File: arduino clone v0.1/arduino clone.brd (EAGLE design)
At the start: 72.9 x 27.6 mm, 47 parts, among them J203 ICSP HEADER, J402 FTDI Breakout Header, U101 ATMEGA328P_TQFP, U301 CH340G, Y101 16MHz, Y301 12MHz

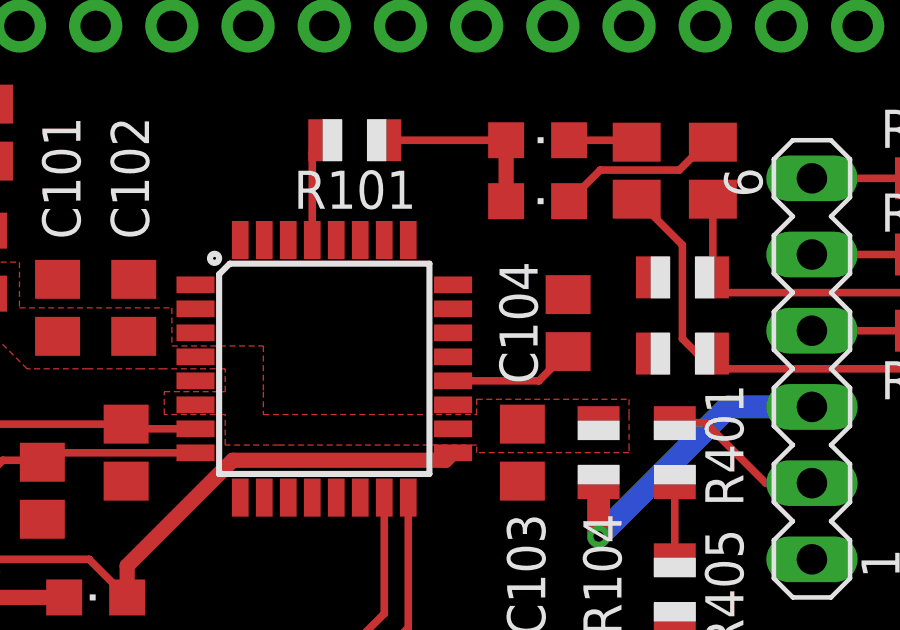
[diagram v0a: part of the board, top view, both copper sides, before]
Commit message: route PP5V0_MCU to UART LEDs
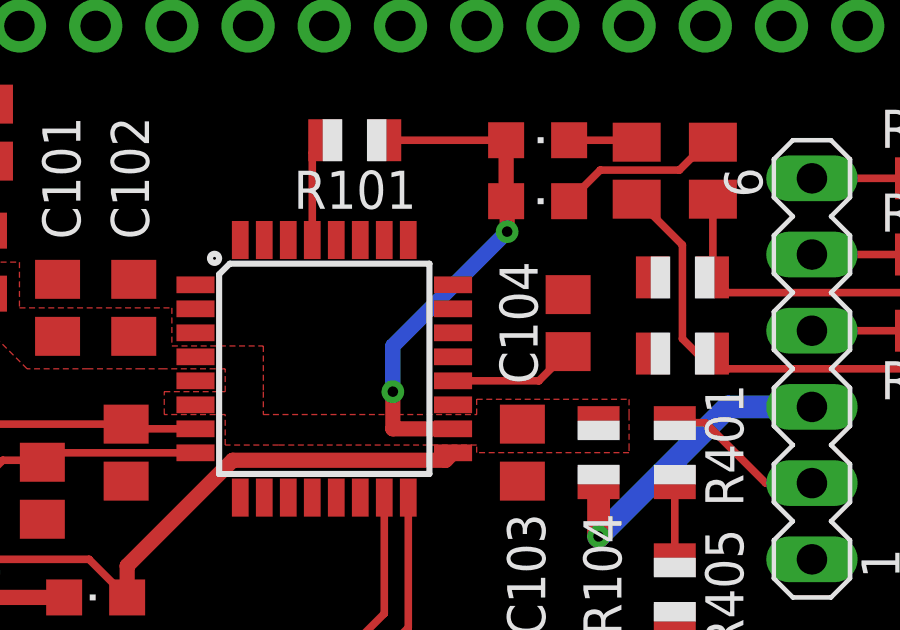
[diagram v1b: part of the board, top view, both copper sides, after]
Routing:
- net PP5V0_MCU: track 26.0 -> 37.2 mm, vias 2 -> 4
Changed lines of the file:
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@@
 <wire x1="40.352" y1="59.69" x2="40.352" y2="57.658" width="0.508" layer="1"/>
 <wire x1="36.306" y1="59.69" x2="40.352" y2="59.69" width="0.254" layer="1"/>
-<wire x1="40.894" y1="50.226" x2="40.352" y2="57.658" width="0" layer="19" extent="1-1"/>
+<wire x1="40.352" y1="57.658" x2="40.386" y2="57.624" width="0.508" layer="1"/>
+<wire x1="40.386" y1="57.624" x2="40.386" y2="56.642" width="0.508" layer="1"/>
+<via x="40.386" y="56.642" extent="1-16" drill="0.35"/>
+<wire x1="40.386" y1="56.642" x2="36.576" y2="52.832" width="0.508" layer="16"/>
+<wire x1="36.576" y1="52.832" x2="36.576" y2="51.308" width="0.508" layer="16"/>
+<via x="36.576" y="51.308" extent="1-16" drill="0.35"/>
+<wire x1="36.576" y1="51.308" x2="36.576" y2="50.07" width="0.508" layer="1"/>
+<wire x1="36.576" y1="50.07" x2="38.5826" y2="50.07" width="0.508" layer="1"/>
 </signal>
 <signal name="GND">

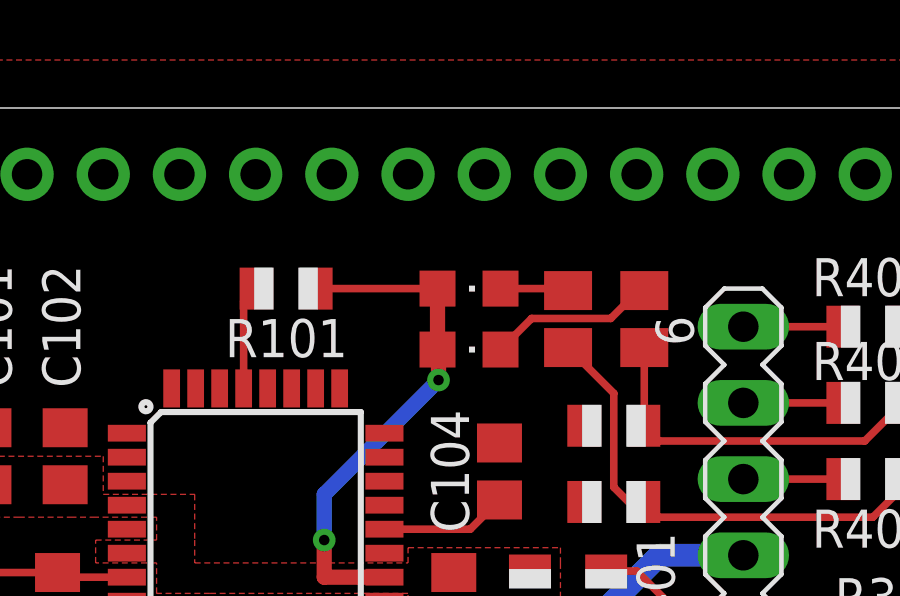
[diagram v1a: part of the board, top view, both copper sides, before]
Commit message: route analog pins 2-5
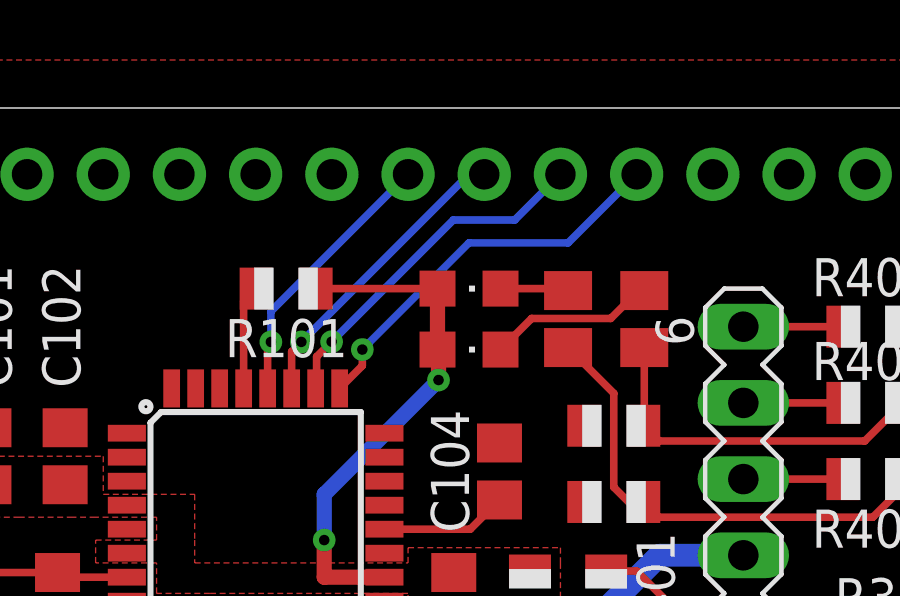
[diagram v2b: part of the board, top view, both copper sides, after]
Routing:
- net MCU_A2: track 0.00 -> 13.2 mm, vias 0 -> 1
- net MCU_A3: track 0.00 -> 11.7 mm, vias 0 -> 1
- net MCU_A4: track 0.00 -> 10.1 mm, vias 0 -> 1
- net MCU_A5: track 0.00 -> 9.08 mm, vias 0 -> 1
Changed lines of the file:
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@@
 <contactref element="R103" pad="2"/>
 <contactref element="J201" pad="1"/>
-<wire x1="32.29" y1="56.3626" x2="45.228" y2="55.118" width="0" layer="19" extent="1-1"/>
+<wire x1="45.228" y1="55.118" x2="32.29" y2="56.3626" width="0" layer="19" extent="1-1"/>
 <wire x1="24.13" y1="40.64" x2="32.29" y2="56.3626" width="0" layer="19" extent="1-1"/>
 </signal>
@@
 <contactref element="U101" pad="25"/>
 <contactref element="J202" pad="10"/>
-<wire x1="37.09" y1="56.3626" x2="46.99" y2="63.5" width="0" layer="19" extent="1-1"/>
+<wire x1="37.846" y1="57.1186" x2="37.846" y2="57.658" width="0.254" layer="1"/>
+<via x="37.846" y="57.658" extent="1-16" drill="0.35"/>
+<wire x1="37.846" y1="57.658" x2="41.402" y2="61.214" width="0.254" layer="16"/>
+<wire x1="41.402" y1="61.214" x2="44.704" y2="61.214" width="0.254" layer="16"/>
+<wire x1="44.704" y1="61.214" x2="46.99" y2="63.5" width="0.254" layer="16"/>
+<wire x1="37.09" y1="56.3626" x2="37.846" y2="57.1186" width="0.254" layer="1"/>
 </signal>
 <signal name="MCU_A5">
 <contactref element="U101" pad="28"/>
 <contactref element="J202" pad="7"/>
-<wire x1="34.69" y1="56.3626" x2="39.37" y2="63.5" width="0" layer="19" extent="1-1"/>
+<wire x1="34.69" y1="56.3626" x2="34.69" y2="57.804" width="0.254" layer="1"/>
+<wire x1="34.69" y1="57.804" x2="34.798" y2="57.912" width="0.254" layer="1"/>
+<via x="34.798" y="57.912" extent="1-16" drill="0.35"/>
+<wire x1="34.798" y1="57.912" x2="34.798" y2="58.928" width="0.254" layer="16"/>
+<wire x1="34.798" y1="58.928" x2="39.37" y2="63.5" width="0.254" layer="16"/>
 </signal>
 <signal name="MCU_A6">
@@
 <contactref element="U101" pad="27"/>
 <contactref element="J202" pad="8"/>
-<wire x1="35.49" y1="56.3626" x2="41.91" y2="63.5" width="0" layer="19" extent="1-1"/>
+<wire x1="35.49" y1="56.3626" x2="35.49" y2="57.588" width="0.254" layer="1"/>
+<wire x1="35.49" y1="57.588" x2="35.814" y2="57.912" width="0.254" layer="1"/>
+<via x="35.814" y="57.912" extent="1-16" drill="0.35"/>
+<wire x1="41.402" y1="63.5" x2="41.91" y2="63.5" width="0.254" layer="16"/>
+<wire x1="35.814" y1="57.912" x2="41.402" y2="63.5" width="0.254" layer="16"/>
 </signal>
 <signal name="MCU_A3">
 <contactref element="U101" pad="26"/>
 <contactref element="J202" pad="9"/>
-<wire x1="36.29" y1="56.3626" x2="44.45" y2="63.5" width="0" layer="19" extent="1-1"/>
+<wire x1="36.29" y1="56.3626" x2="36.322" y2="56.3946" width="0.254" layer="1"/>
+<wire x1="36.322" y1="56.3946" x2="36.322" y2="57.4192375" width="0.254" layer="1"/>
+<wire x1="36.82238125" y1="57.91961875" x2="36.322" y2="57.4192375" width="0.254" layer="1"/>
+<via x="36.82238125" y="57.91961875" extent="1-16" drill="0.35"/>
+<wire x1="36.82238125" y1="57.91961875" x2="40.8787625" y2="61.976" width="0.254" layer="16"/>
+<wire x1="40.8787625" y1="61.976" x2="42.926" y2="61.976" width="0.254" layer="16"/>
+<wire x1="42.926" y1="61.976" x2="44.45" y2="63.5" width="0.254" layer="16"/>
 </signal>
 <signal name="MCU_D2">
@@
 <contactref element="R102" pad="2"/>
 <contactref element="J201" pad="2"/>
-<wire x1="33.09" y1="56.3626" x2="45.228" y2="52.578" width="0" layer="19" extent="1-1"/>
+<wire x1="45.228" y1="52.578" x2="33.09" y2="56.3626" width="0" layer="19" extent="1-1"/>
 <wire x1="26.67" y1="40.64" x2="33.09" y2="56.3626" width="0" layer="19" extent="1-1"/>
 </signal>

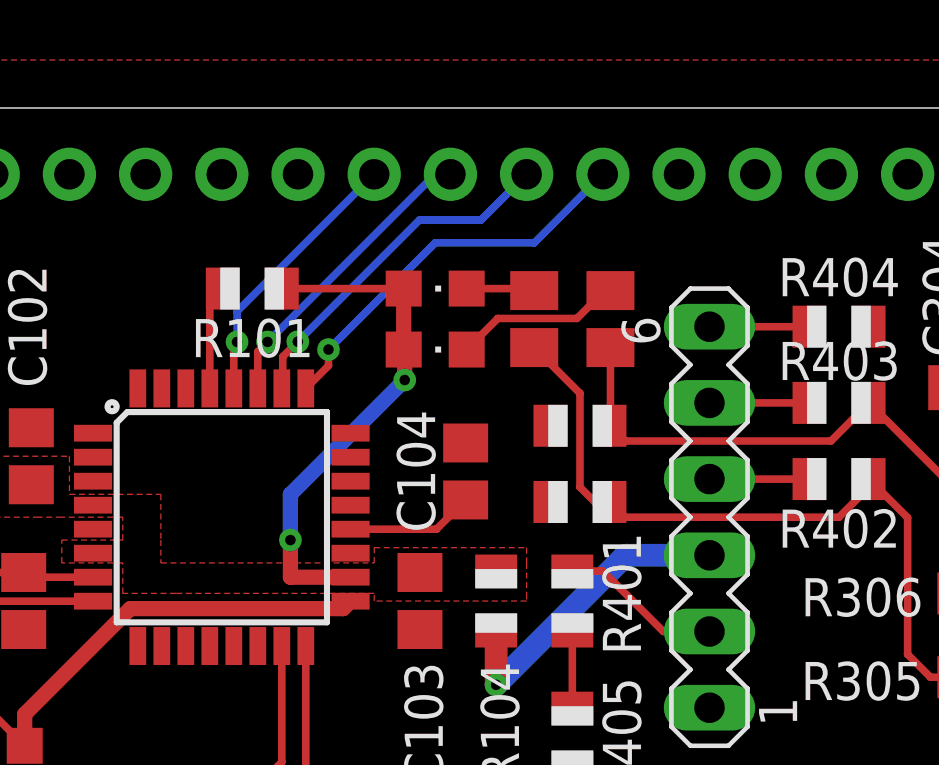
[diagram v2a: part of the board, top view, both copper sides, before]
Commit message: connect rest of analog pins
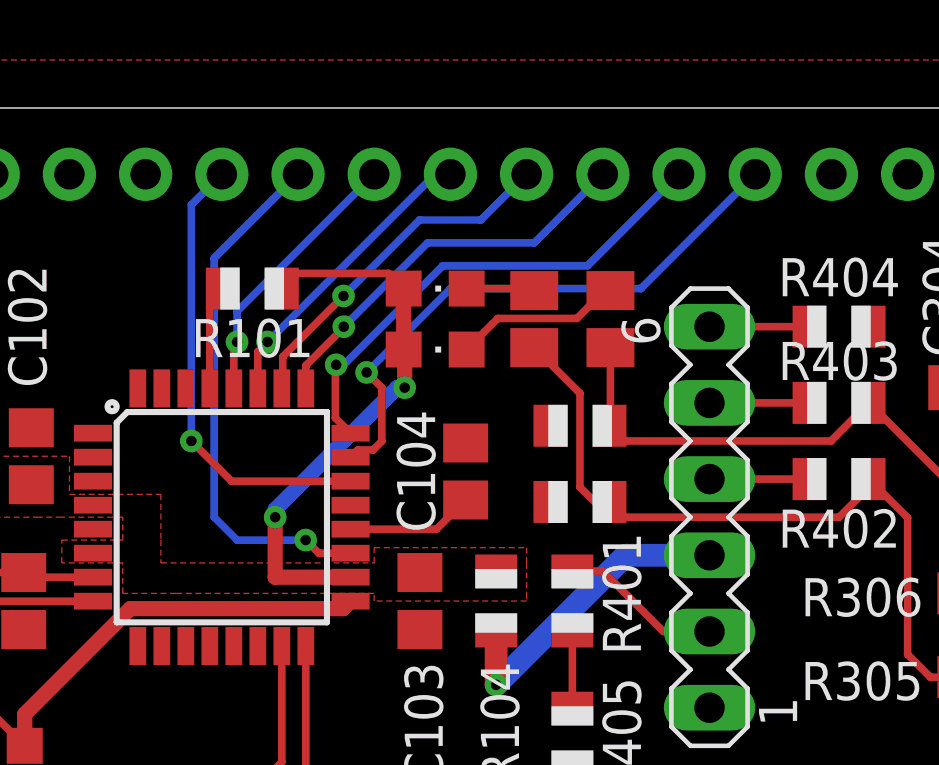
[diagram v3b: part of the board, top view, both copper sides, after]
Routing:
- net MCU_A0: track 0.00 -> 19.5 mm, vias 0 -> 1
- net MCU_A6: track 0.00 -> 17.6 mm, vias 0 -> 1
- net MCU_A1: track 0.00 -> 16.6 mm, vias 0 -> 1
- net MCU_A7: track 0.00 -> 15.2 mm, vias 0 -> 1
- net PP5V0_MCU: track 37.2 -> 38.5 mm
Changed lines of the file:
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@@
 <wire x1="16.51" y1="54.61" x2="21.59" y2="54.61" width="0.254" layer="16"/>
 <wire x1="40.352" y1="59.69" x2="40.352" y2="57.658" width="0.508" layer="1"/>
-<wire x1="36.306" y1="59.69" x2="40.352" y2="59.69" width="0.254" layer="1"/>
+<wire x1="36.814" y1="60.198" x2="39.844" y2="60.198" width="0.254" layer="1"/>
 <wire x1="40.352" y1="57.658" x2="40.386" y2="57.624" width="0.508" layer="1"/>
-<wire x1="40.386" y1="57.624" x2="40.386" y2="56.642" width="0.508" layer="1"/>
-<via x="40.386" y="56.642" extent="1-16" drill="0.35"/>
-<wire x1="40.386" y1="56.642" x2="36.576" y2="52.832" width="0.508" layer="16"/>
-<wire x1="36.576" y1="52.832" x2="36.576" y2="51.308" width="0.508" layer="16"/>
-<via x="36.576" y="51.308" extent="1-16" drill="0.35"/>
-<wire x1="36.576" y1="51.308" x2="36.576" y2="50.07" width="0.508" layer="1"/>
-<wire x1="36.576" y1="50.07" x2="38.5826" y2="50.07" width="0.508" layer="1"/>
+<wire x1="40.386" y1="57.624" x2="40.386" y2="56.388" width="0.508" layer="1"/>
+<via x="40.386" y="56.388" extent="1-16" drill="0.35"/>
+<wire x1="40.132" y1="56.388" x2="36.068" y2="52.324" width="0.508" layer="16"/>
+<wire x1="36.068" y1="52.324" x2="36.068" y2="52.07" width="0.508" layer="16"/>
+<via x="36.068" y="52.07" extent="1-16" drill="0.35"/>
+<wire x1="36.068" y1="52.07" x2="36.068" y2="50.07" width="0.508" layer="1"/>
+<wire x1="36.068" y1="50.07" x2="38.5826" y2="50.07" width="0.508" layer="1"/>
+<wire x1="36.306" y1="59.69" x2="36.814" y2="60.198" width="0.254" layer="1"/>
+<wire x1="39.844" y1="60.198" x2="40.352" y2="59.69" width="0.254" layer="1"/>
+<wire x1="40.386" y1="56.388" x2="40.132" y2="56.388" width="0.508" layer="16"/>
 </signal>
 <signal name="GND">
@@
 <contactref element="R103" pad="2"/>
 <contactref element="J201" pad="1"/>
-<wire x1="45.228" y1="55.118" x2="32.29" y2="56.3626" width="0" layer="19" extent="1-1"/>
+<wire x1="32.29" y1="56.3626" x2="45.228" y2="55.118" width="0" layer="19" extent="1-1"/>
 <wire x1="24.13" y1="40.64" x2="32.29" y2="56.3626" width="0" layer="19" extent="1-1"/>
 </signal>
@@
 <contactref element="U101" pad="23"/>
 <contactref element="J202" pad="12"/>
-<wire x1="38.5826" y1="54.07" x2="52.07" y2="63.5" width="0" layer="19" extent="1-1"/>
+<wire x1="38.5826" y1="54.07" x2="38.8238" y2="54.3112" width="0.254" layer="1"/>
+<wire x1="38.8238" y1="54.3112" x2="39.33333125" y2="54.3112" width="0.254" layer="1"/>
+<wire x1="39.33333125" y1="54.3112" x2="39.624" y2="54.60186875" width="0.254" layer="1"/>
+<wire x1="39.624" y1="56.388" x2="39.116" y2="56.896" width="0.254" layer="1"/>
+<via x="39.116" y="56.896" extent="1-16" drill="0.35"/>
+<wire x1="39.116" y1="56.896" x2="41.91" y2="59.69" width="0.254" layer="16"/>
+<wire x1="48.26" y1="59.69" x2="52.07" y2="63.5" width="0.254" layer="16"/>
+<wire x1="39.624" y1="54.60186875" x2="39.624" y2="56.388" width="0.254" layer="1"/>
+<wire x1="41.91" y1="59.69" x2="48.26" y2="59.69" width="0.254" layer="16"/>
 </signal>
 <signal name="MCU_A1">
 <contactref element="U101" pad="24"/>
 <contactref element="J202" pad="11"/>
-<wire x1="38.5826" y1="54.87" x2="49.53" y2="63.5" width="0" layer="19" extent="1-1"/>
+<wire x1="38.0746" y1="55.378" x2="38.0746" y2="57.1246" width="0.254" layer="1"/>
+<via x="38.1" y="57.15" extent="1-16" drill="0.35"/>
+<wire x1="38.354" y1="57.15" x2="38.1" y2="57.15" width="0.254" layer="16"/>
+<wire x1="38.354" y1="57.15" x2="41.656" y2="60.452" width="0.254" layer="16"/>
+<wire x1="46.482" y1="60.452" x2="41.656" y2="60.452" width="0.254" layer="16"/>
+<wire x1="49.53" y1="63.5" x2="46.482" y2="60.452" width="0.254" layer="16"/>
+<wire x1="38.5826" y1="54.87" x2="38.0746" y2="55.378" width="0.254" layer="1"/>
+<wire x1="38.0746" y1="57.1246" x2="38.1" y2="57.15" width="0.254" layer="1"/>
 </signal>
 <signal name="MCU_A2">
 <contactref element="U101" pad="25"/>
 <contactref element="J202" pad="10"/>
-<wire x1="37.846" y1="57.1186" x2="37.846" y2="57.658" width="0.254" layer="1"/>
-<via x="37.846" y="57.658" extent="1-16" drill="0.35"/>
-<wire x1="37.846" y1="57.658" x2="41.402" y2="61.214" width="0.254" layer="16"/>
-<wire x1="41.402" y1="61.214" x2="44.704" y2="61.214" width="0.254" layer="16"/>
+<wire x1="38.354" y1="58.3886" x2="38.354" y2="58.42" width="0.254" layer="1"/>
+<via x="38.354" y="58.42" extent="1-16" drill="0.35"/>
+<wire x1="38.354" y1="58.42" x2="41.148" y2="61.214" width="0.254" layer="16"/>
+<wire x1="41.148" y1="61.214" x2="44.704" y2="61.214" width="0.254" layer="16"/>
 <wire x1="44.704" y1="61.214" x2="46.99" y2="63.5" width="0.254" layer="16"/>
-<wire x1="37.09" y1="56.3626" x2="37.846" y2="57.1186" width="0.254" layer="1"/>
+<wire x1="37.09" y1="57.1246" x2="38.354" y2="58.3886" width="0.254" layer="1"/>
+<wire x1="37.09" y1="56.3626" x2="37.09" y2="57.1246" width="0.254" layer="1"/>
 </signal>
 <signal name="MCU_A5">
@@
 <contactref element="U101" pad="19"/>
 <contactref element="J202" pad="6"/>
-<wire x1="38.5826" y1="50.87" x2="36.83" y2="63.5" width="0" layer="19" extent="1-1"/>
+<wire x1="38.5826" y1="50.87" x2="37.522" y2="50.87" width="0.254" layer="1"/>
+<wire x1="37.522" y1="50.87" x2="37.084" y2="51.308" width="0.254" layer="1"/>
+<via x="37.084" y="51.308" extent="1-16" drill="0.35"/>
+<wire x1="37.084" y1="51.308" x2="34.798" y2="51.308" width="0.254" layer="16"/>
+<wire x1="34.798" y1="51.308" x2="34.036" y2="52.07" width="0.254" layer="16"/>
+<wire x1="34.036" y1="60.706" x2="36.83" y2="63.5" width="0.254" layer="16"/>
+<wire x1="34.036" y1="52.07" x2="34.036" y2="60.706" width="0.254" layer="16"/>
 </signal>
 <signal name="MCU_A7">
 <contactref element="U101" pad="22"/>
 <contactref element="J202" pad="5"/>
-<wire x1="38.5826" y1="53.27" x2="34.29" y2="63.5" width="0" layer="19" extent="1-1"/>
+<wire x1="38.5826" y1="53.27" x2="38.5826" y2="53.2826" width="0.254" layer="1"/>
+<wire x1="38.5826" y1="53.27" x2="34.614" y2="53.27" width="0.254" layer="1"/>
+<wire x1="34.614" y1="53.27" x2="33.274" y2="54.61" width="0.254" layer="1"/>
+<via x="33.274" y="54.61" extent="1-16" drill="0.35"/>
+<wire x1="33.274" y1="54.61" x2="33.274" y2="62.484" width="0.254" layer="16"/>
+<wire x1="33.274" y1="62.484" x2="34.29" y2="63.5" width="0.254" layer="16"/>
 </signal>
 <signal name="MCU_A4">
@@
 <wire x1="36.29" y1="56.3626" x2="36.322" y2="56.3946" width="0.254" layer="1"/>
 <wire x1="36.322" y1="56.3946" x2="36.322" y2="57.4192375" width="0.254" layer="1"/>
-<wire x1="36.82238125" y1="57.91961875" x2="36.322" y2="57.4192375" width="0.254" layer="1"/>
-<via x="36.82238125" y="57.91961875" extent="1-16" drill="0.35"/>
-<wire x1="36.82238125" y1="57.91961875" x2="40.8787625" y2="61.976" width="0.254" layer="16"/>
+<wire x1="38.34638125" y1="59.44361875" x2="36.322" y2="57.4192375" width="0.254" layer="1"/>
+<via x="38.34638125" y="59.44361875" extent="1-16" drill="0.35"/>
+<wire x1="38.34638125" y1="59.44361875" x2="40.8787625" y2="61.976" width="0.254" layer="16"/>
 <wire x1="40.8787625" y1="61.976" x2="42.926" y2="61.976" width="0.254" layer="16"/>
 <wire x1="42.926" y1="61.976" x2="44.45" y2="63.5" width="0.254" layer="16"/>
@@
 <contactref element="U101" pad="32"/>
 <contactref element="J201" pad="5"/>
-<wire x1="31.49" y1="56.3626" x2="34.29" y2="40.64" width="0" layer="19" extent="1-1"/>
+<wire x1="34.29" y1="40.64" x2="31.49" y2="56.3626" width="0" layer="19" extent="1-1"/>
 </signal>
 <signal name="MCU_D3">
@@
 <contactref element="R102" pad="2"/>
 <contactref element="J201" pad="2"/>
-<wire x1="45.228" y1="52.578" x2="33.09" y2="56.3626" width="0" layer="19" extent="1-1"/>
+<wire x1="33.09" y1="56.3626" x2="45.228" y2="52.578" width="0" layer="19" extent="1-1"/>
 <wire x1="26.67" y1="40.64" x2="33.09" y2="56.3626" width="0" layer="19" extent="1-1"/>
 </signal>
